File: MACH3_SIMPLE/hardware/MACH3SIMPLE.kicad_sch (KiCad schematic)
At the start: 0 parts

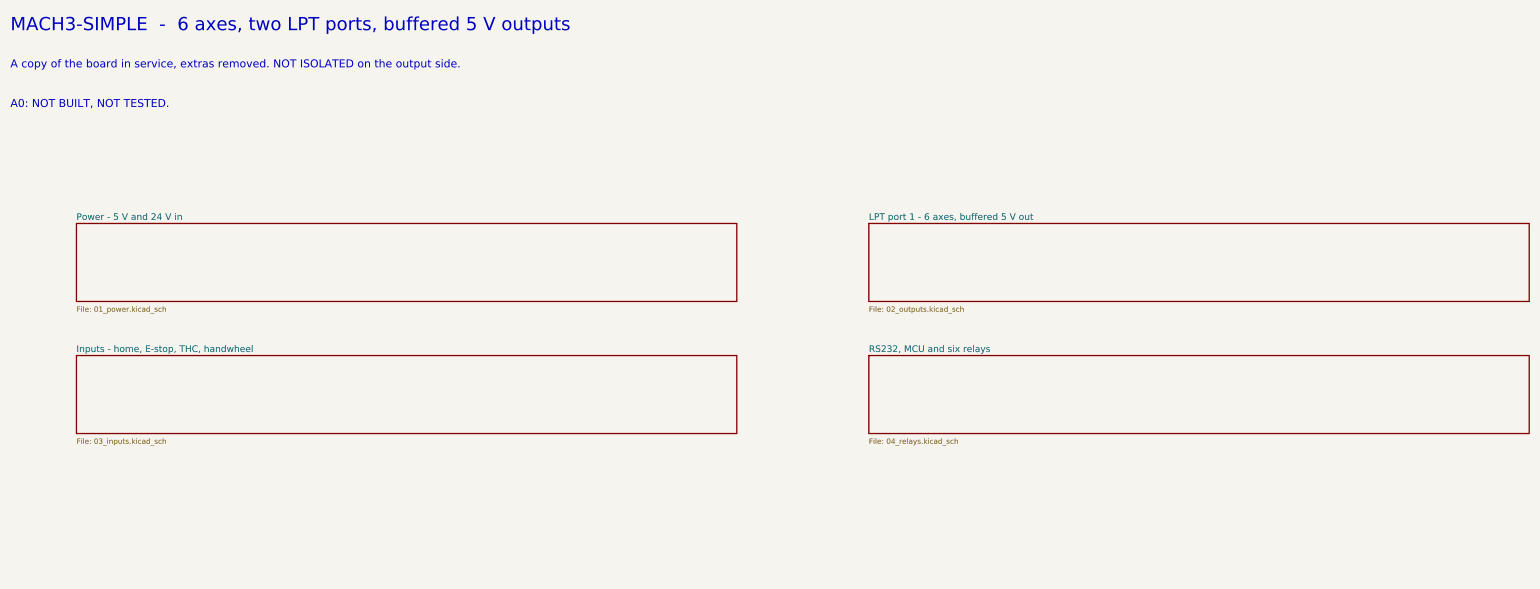
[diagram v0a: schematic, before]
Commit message: MACH3-SIMPLE A1: on-board 5 V, isolated VFD port, four A0 fixes
Power: the 5 V input terminal is gone. An LM2596S-5.0 buck makes +5V from
V24, and the whole supply sits in the top-right corner beside the 24 V
terminal, away from the MCU crystal and the port lines.

Spindle: new J5 (AVI ACM FWD REV DCM). Port 2 pins 7/8/9 go through a
74HC14 to a PC847; the VFD side runs from a B2412S isolated module with a
78L05 reference, a two-pole RC filter and an LM358 trimmed to 10.0 V. It
has its own SP_ACM pour, and the board is routed in two passes so no
board-side copper enters it; autoroute.py barrier checks that and fab.sh
refuses Gerbers without it.

Fixes to A0:
- Q1-Q6 had drain and source swapped; every relay was stuck on through
  the body diode. check_design.py now checks MOSFET orientation.
- The top-edge legends were reversed (+24 over 0V, +5 over MPG B, EMG over
  X home). Signals now follow the printed order, one word per screw.
- PC847 was on a SOIC-16 footprint no PC847 fits; now SMD DIP-16.
- The promised reverse diodes across the input opto LEDs were missing;
  added as D20-D25, with the input channels laid out per screw.

ERC 0, structural checks pass, DRC 0 errors / 0 unconnected / 0 parity,
barrier clean. Not built or powered.

Co-Authored-By: Claude Opus 5.5 <noreply@anthropic.com>
Claude-Session: https://claude.ai/code/session_01MByiLT2xCcbGPkgCYQy33q
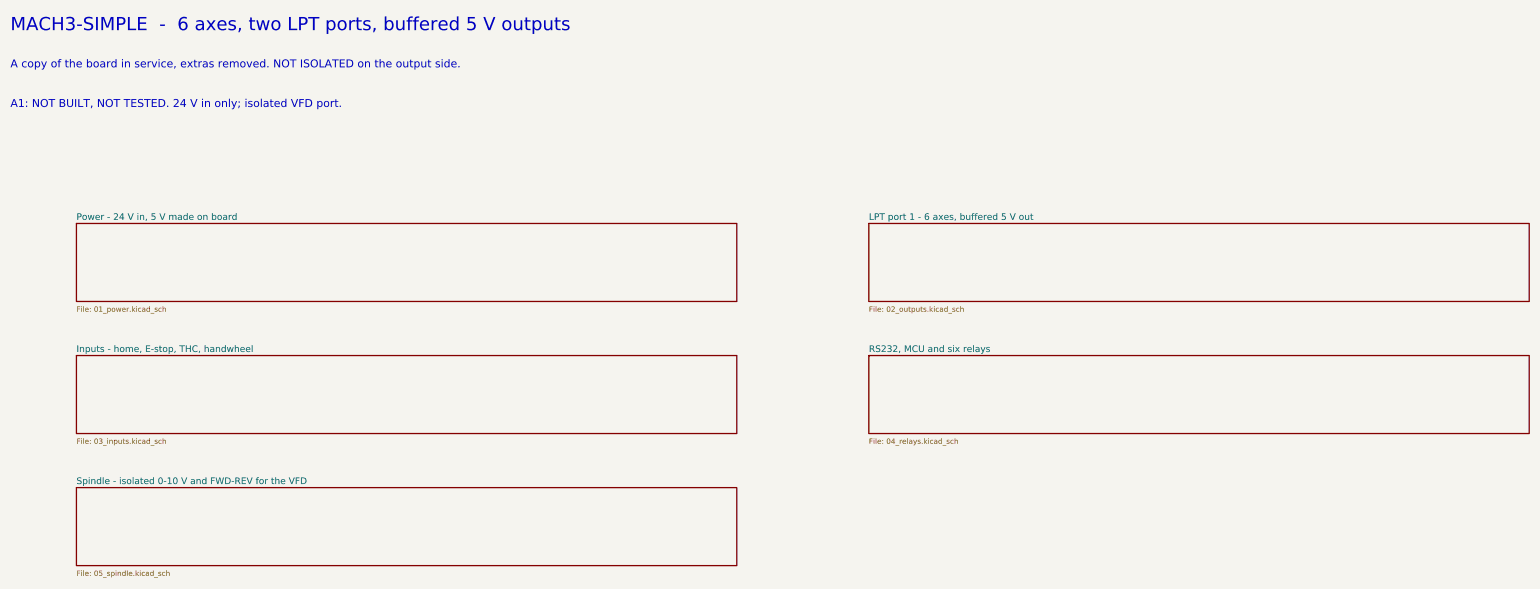
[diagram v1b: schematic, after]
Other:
- sheet Power - 5 V and 24 V in renamed Power - 24 V in, 5 V made on board
- added sheet Spindle - isolated 0-10 V and FWD-REV for the VFD (05_spindle.kicad_sch)
- note added: "A1: NOT BUILT, NOT TESTED. 24 V in only; isolated VFD port."
- note removed: "A0: NOT BUILT, NOT TESTED."
